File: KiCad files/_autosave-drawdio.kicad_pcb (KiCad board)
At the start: 2 copper layers, 94 x 22 mm, 26 parts, among them P1 CONN_01X01, P10 CONN_01X02, P2 CONN_01X01, P3 CONN_01X01, P4 CONN_01X02, P5 CONN_01X01, P6 CONN_01X01, P7 CONN_01X01, P9 CONN_02X04, Q1 BC558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

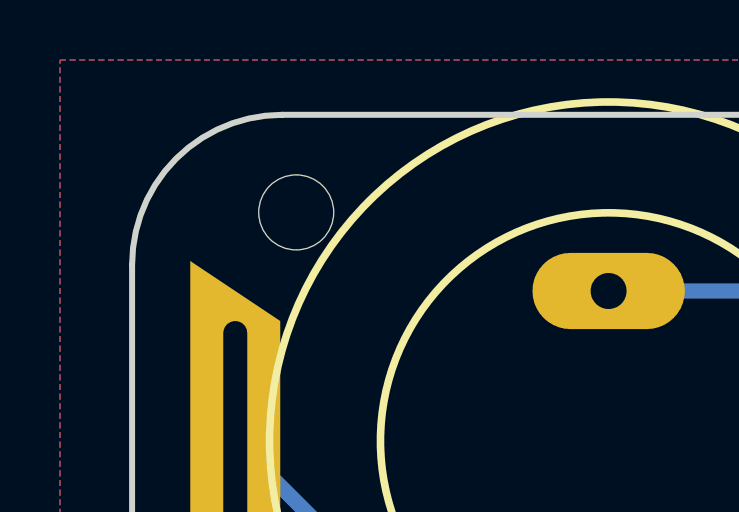
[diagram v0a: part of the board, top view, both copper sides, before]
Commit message: files moved to folders
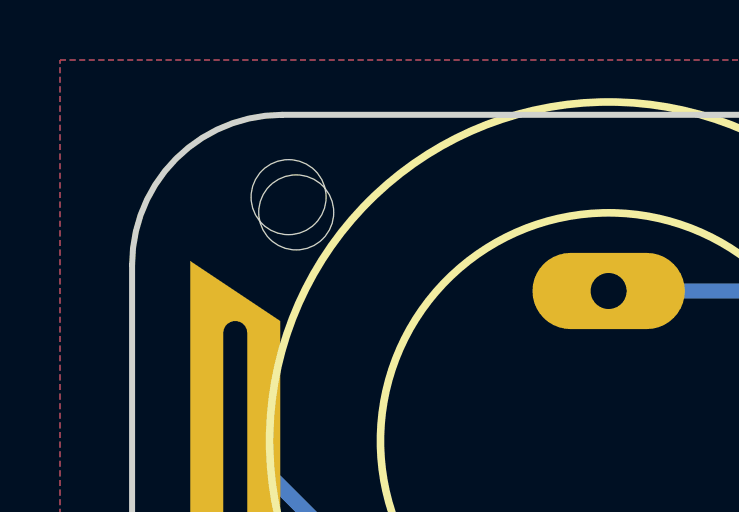
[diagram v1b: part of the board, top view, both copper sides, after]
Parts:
- added P7: CONN_01X01, Mounting_Holes:MountingHole_2-5mm, F.Cu at (62.0, 78.2)
